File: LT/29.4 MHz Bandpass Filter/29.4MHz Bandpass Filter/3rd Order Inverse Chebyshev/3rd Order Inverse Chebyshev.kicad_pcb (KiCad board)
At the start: 2 copper layers, 83.3 x 25 mm, 22 parts, among them J1 Conn_Coaxial, J2 Conn_Coaxial

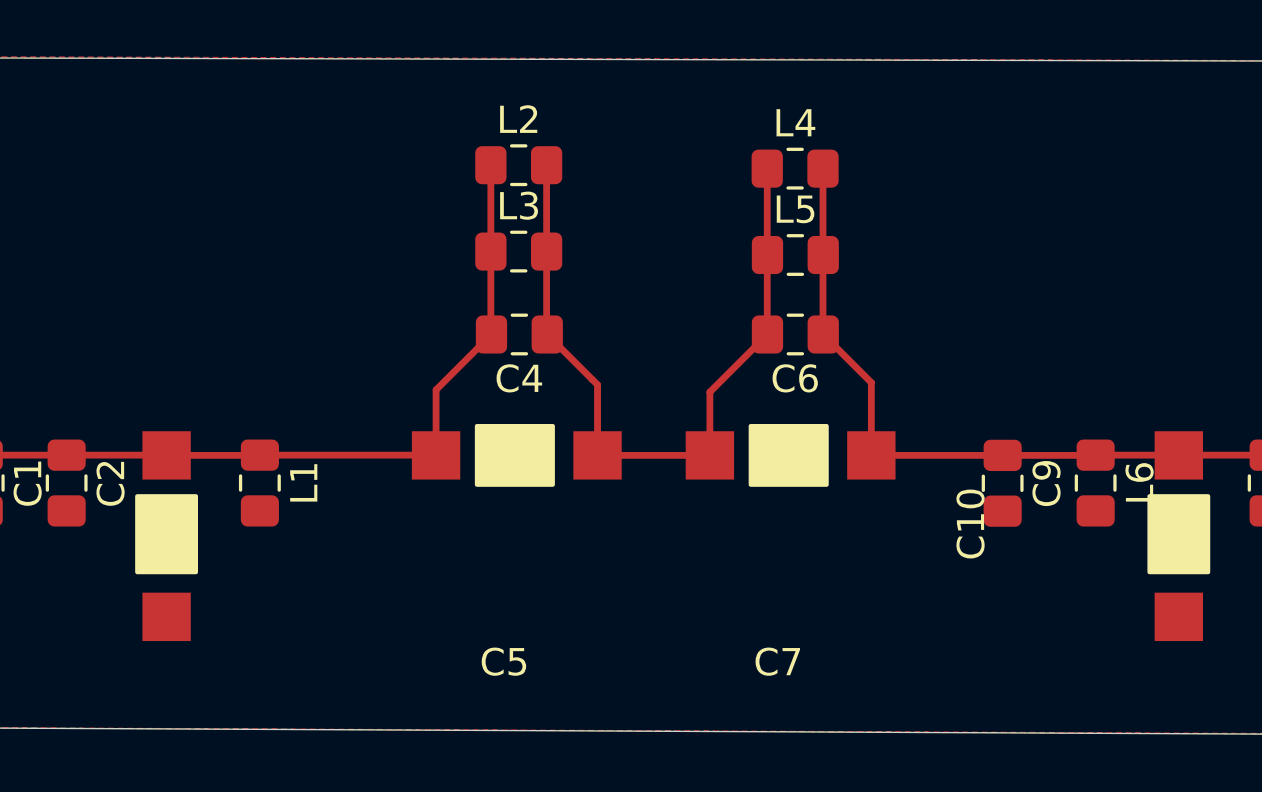
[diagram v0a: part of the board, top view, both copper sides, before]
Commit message: Changes to 29.4 MHz Bandpass Filter
I made some changes to my best filter design, allowing for series inductors
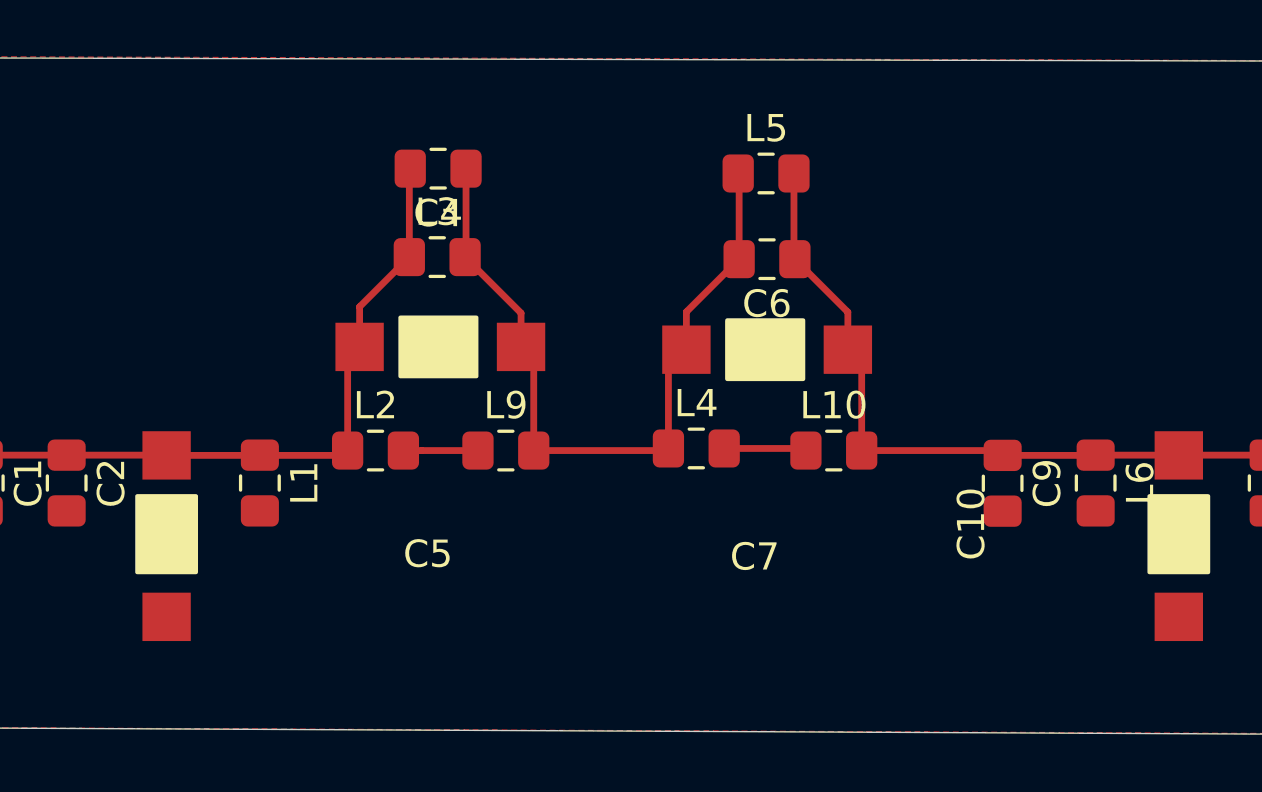
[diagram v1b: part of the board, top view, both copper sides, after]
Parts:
- added L10: 75nH, Inductor_SMD:L_0805_2012Metric_Pad1.15x1.40mm_HandSolder, F.Cu at (158.9, 43.1)
- added L9: 6.8nH, Inductor_SMD:L_0805_2012Metric_Pad1.15x1.40mm_HandSolder, F.Cu at (146.8, 43.1)
- L4: value 1.6uH -> 1.5uH
- moved L2 11.7 mm to (142.0, 43.1)
- moved L4 10.9 mm to (153.8, 43.1)
- moved C4 6.79 mm to (144.3, 32.8)
- moved C5 4.88 mm to (144.0, 39.3)
- moved C7 3.98 mm to (156.0, 39.4)
- moved L5 3.18 mm to (156.4, 32.9)
- moved L3 3.00 mm to (144.3, 36.0)
- moved C6 2.96 mm to (156.4, 36.1)
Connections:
- L2 pad 2: Net-(C4-Pad1) -> Net-(L2-Pad2)
- L4 pad 2: Net-(C10-Pad1) -> Net-(L10-Pad1)
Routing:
- net Net-(C1-Pad1): track 34.0 -> 30.6 mm
- net Net-(L10-Pad1): track 0.00 -> 3.04 mm
- net Net-(L2-Pad2): track 0.00 -> 2.74 mm
- net Net-(C4-Pad1): track 27.0 -> 27.6 mm

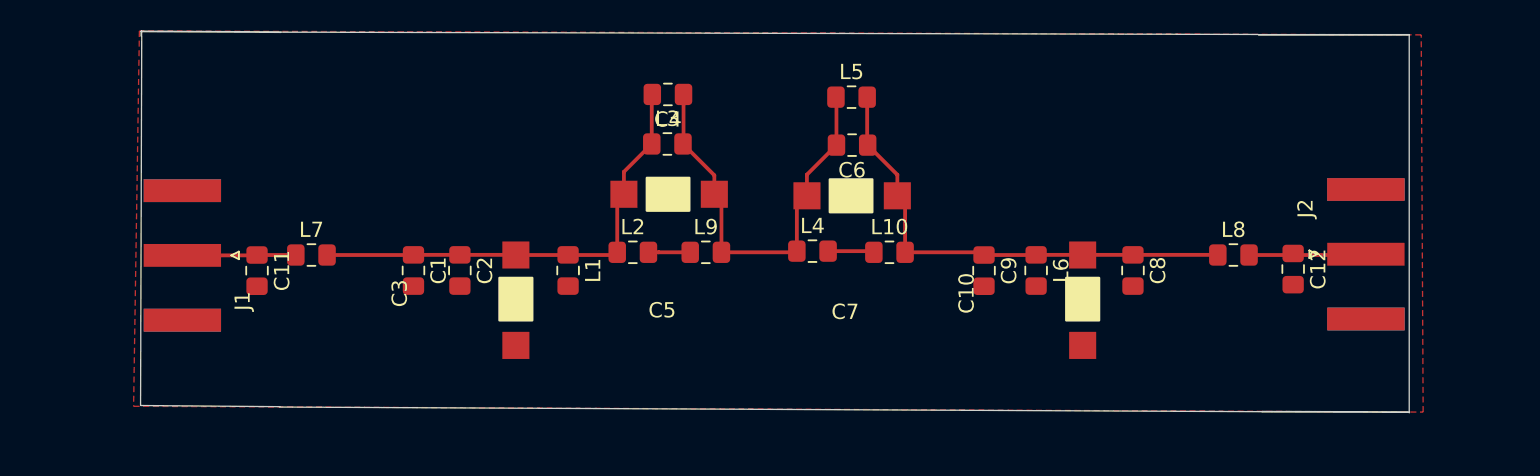
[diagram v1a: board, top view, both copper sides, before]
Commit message: Final Banpdass Filter Design
I updated the Bandpass Filter with the pads that are no connect or shorted.
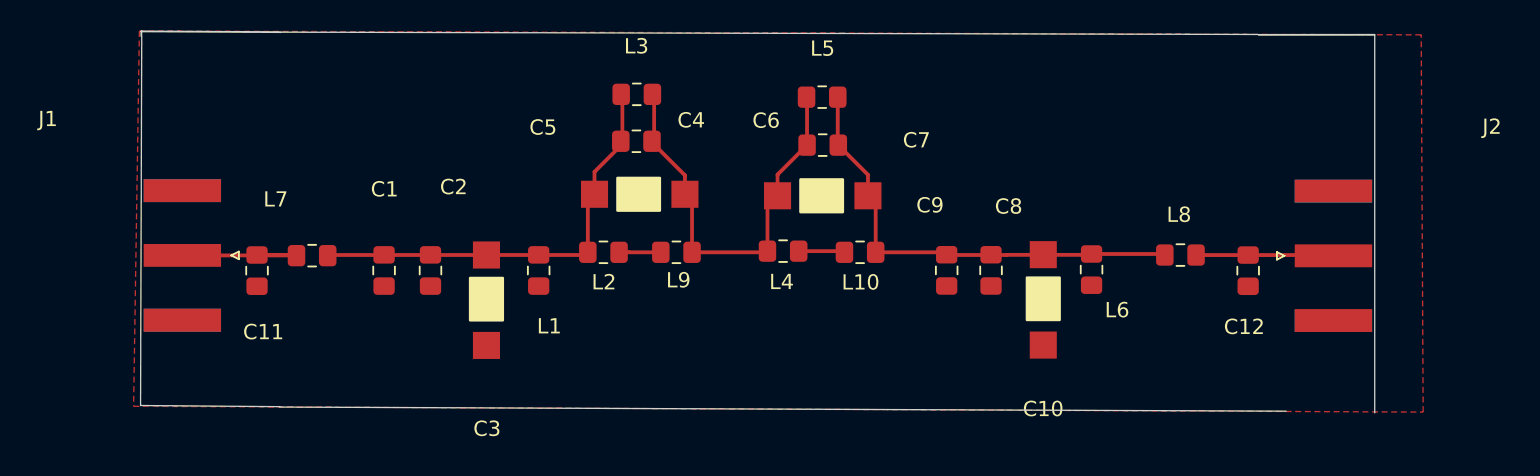
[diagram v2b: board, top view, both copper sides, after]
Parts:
- C10, C3, C5, C7: value C_Variable -> No Connect
- C11: value 58.44pF -> No Connect
- C12: value 85.29pF -> No Connect
- L10: value 75nH -> 72nH
- L3, L5: value L -> No Connect
- L7: value 119.7nH -> Shorted Connection
- L8: value 120nH -> Shorted Connection
- moved C8 9.32 mm to (165.6, 44.3)
- moved L3 3.83 mm to (142.3, 32.8)
- moved C4 3.70 mm to (142.3, 35.8)
- moved L6 3.64 mm to (172.2, 44.3)
- moved L8 3.48 mm to (178.0, 43.3)
- moved C12 2.96 mm to (182.4, 44.3)
- moved C10 2.59 mm to (169.0, 45.8)
- moved C9 2.45 mm to (162.7, 44.3)
- moved J2 2.13 mm to (188.0, 43.4)
- moved C1 1.93 mm to (125.7, 44.3)
- moved C2 1.93 mm to (128.8, 44.3)
- moved C3 1.93 mm to (132.4, 45.8)
- moved C5 1.93 mm to (142.0, 39.3)
- moved C6 1.93 mm to (154.5, 36.1)
- moved C7 1.93 mm to (154.1, 39.4)
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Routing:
- net Net-(C11-Pad1): track 7.46 -> 10.0 mm
- net Net-(C1-Pad1): track 30.6 -> 28.7 mm
- net Net-(C10-Pad1): track 31.8 -> 30.3 mm
- net Net-(C12-Pad1): track 7.69 -> 9.04 mm
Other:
- board size 83.3 x 25 mm -> 81 x 25 mm
